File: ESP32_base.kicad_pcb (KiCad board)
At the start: 2 copper layers, 112 x 54.9 mm, 36 parts, among them J1 Conn_01x16_Socket, J2 Conn_01x16_Socket, J3 Conn_01x04_Socket, J4 USB_C_Receptacle_USB2.0_14P, J5 KH-IPEXA-SMAKWE-B080H, SW1 boot, SW2 reset, U1 ADT7310TRZ, U2 AP63203WU, U3 ESP32-C5-WROOM-1U-N8-R4

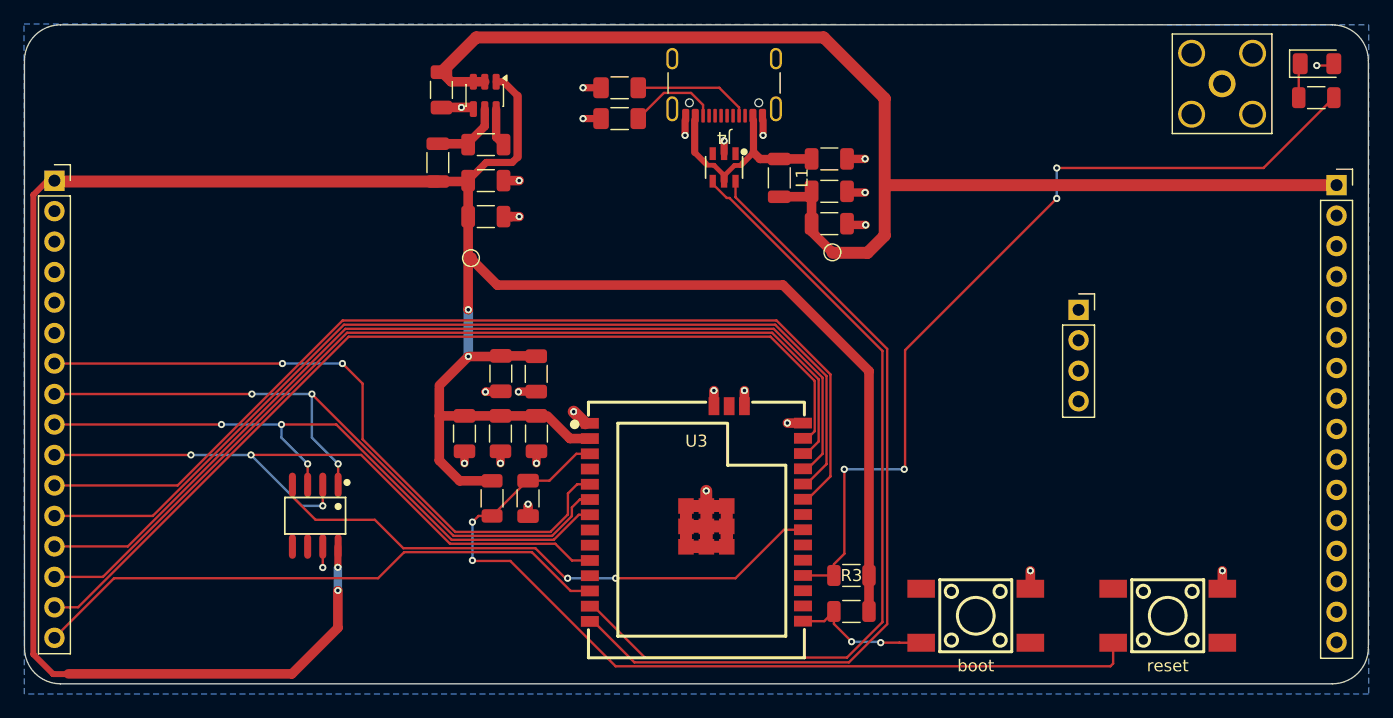
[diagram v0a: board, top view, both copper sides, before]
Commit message: fixed signal width at 0.3mm
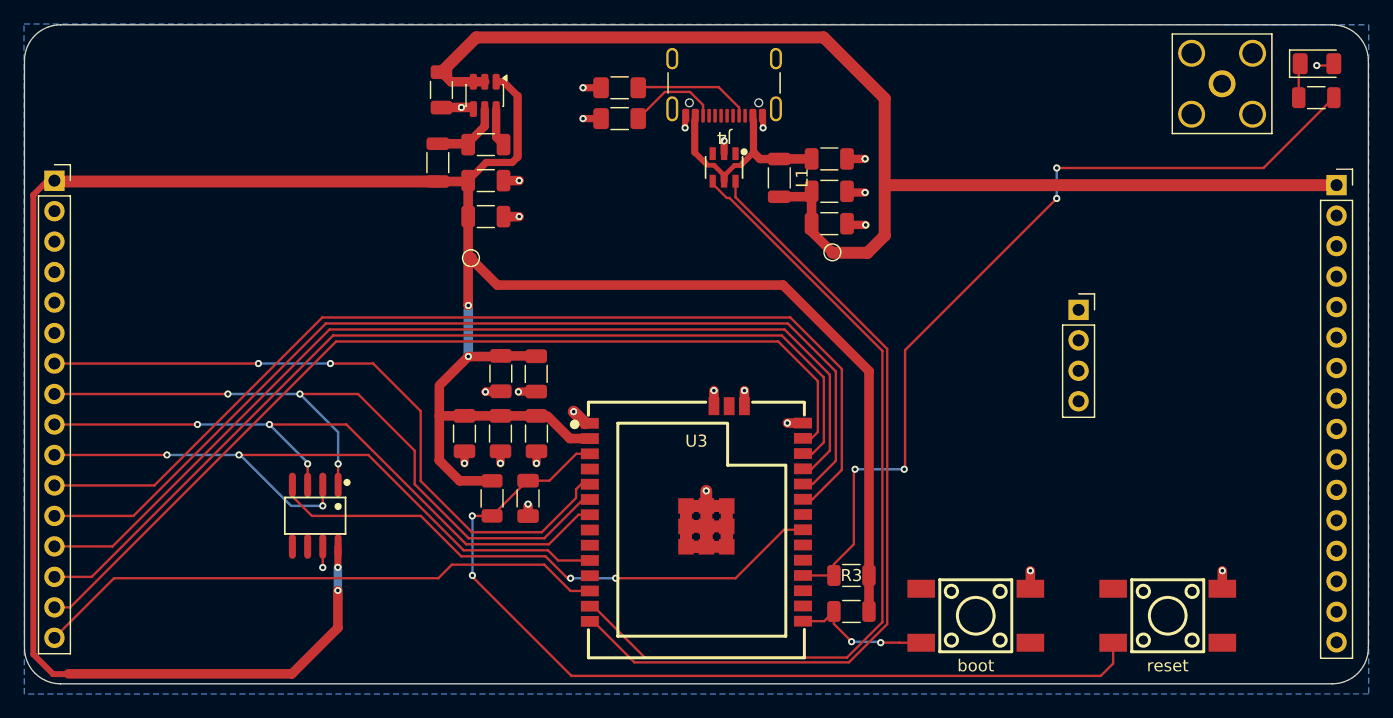
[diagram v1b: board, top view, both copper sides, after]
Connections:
- C1 pad 1: /USB_D+ -> Net-(C1-Pad1)
- J4 pad A4: /USB_D+ -> Net-(C1-Pad1)
- J4 pad A9: /USB_D+ -> Net-(C1-Pad1)
- J4 pad B4: /USB_D+ -> Net-(C1-Pad1)
- J4 pad B9: /USB_D+ -> Net-(C1-Pad1)
- L1 pad 1: /USB_D+ -> Net-(C1-Pad1)
- TVS1 pad 5: /USB_D+ -> Net-(C1-Pad1)
- TVS1 pad 6: /USB_D+ -> /USB_D-
- U3 pad 14: /USB_D+ -> /USB_D-
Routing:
- net /USB_D+: track 156.6 -> 69.6 mm
- net /USB_D-: track 0.00 -> 69.4 mm
- net Net-(C1-Pad1): track 0.00 -> 17.7 mm
- net /TP_IRQ: track 83.4 -> 85.5 mm
- net /TP_CS: track 82.4 -> 84.1 mm
- net Net-(U3-EN): track 73.9 -> 75.6 mm
- net /SPI_SCK: track 59.7 -> 61.3 mm
- net GND: track 63.2 -> 62.0 mm
- net /LCD_RST: track 81.3 -> 82.5 mm
- net /SPI_MISO: track 57.8 -> 58.8 mm
- net /SPI_MOSI: track 55.4 -> 56.3 mm
- net /LCD_DC: track 48.9 -> 48.1 mm
- net /LCD_CS: track 80.3 -> 81.1 mm

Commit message: wip
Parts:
- TVS1: footprint easyeda2kicad:SOT-23-6_L2.9-W1.6-P0.95-LS2.8-BL -> Package_TO_SOT_SMD:SOT-23-6
- turned TVS1 to -90 degrees
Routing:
- net /SPI_MISO: track 58.8 -> 64.9 mm
- net /SPI_MOSI: track 56.3 -> 62.4 mm
- net /SPI_SCK: track 61.3 -> 65.8 mm

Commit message: production ready #2
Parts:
- J4: value USB_C_Receptacle_USB2.0_14P -> USB_C_Receptacle_USB2.0_16P
- moved J4 0.20 mm to (141.9, 195.7)
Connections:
- J4 pad A8: (no net) -> unconnected-(J4-SBU1-PadA8)
- J4 pad B8: (no net) -> unconnected-(J4-SBU2-PadB8)
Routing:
- net Net-(J4-D+-PadA6): track 0.00 -> 6.13 mm
- net Net-(J4-D--PadA7): track 0.00 -> 5.80 mm

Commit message: wip
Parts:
- removed C10: 10uF, Capacitor_SMD:C_1206_3216Metric
- removed C11: 100nF, Capacitor_SMD:C_1206_3216Metric
- removed test_point1: 5V, TestPoint:TestPoint_Pad_D1.0mm
- removed test_point2: 3.3V, TestPoint:TestPoint_Pad_D1.0mm
- moved L1 4.67 mm to (150.8, 202.9), turned to 0 degrees
- moved L2 4.15 mm to (122.0, 204.6), turned to 180 degrees
- moved C1 3.01 mm to (150.8, 200.2)
- moved C6 2.20 mm to (122.0, 207.2)
- moved C7 1.80 mm to (122.0, 209.8)
- moved C13 0.71 mm to (120.2, 225.4), turned to -90 degrees
- moved C8 0.71 mm to (126.2, 225.4), turned to -90 degrees
- moved C9 0.71 mm to (123.2, 225.4), turned to -90 degrees
- moved C3 0.38 mm to (150.8, 208.2)
- moved C2 0.36 mm to (150.8, 205.5)
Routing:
- net Net-(C1-Pad1): track 17.9 -> 26.6 mm, vias 0 -> 2
- net +3.3V: track 226.5 -> 223.0 mm
- net GND: track 62.0 -> 64.2 mm, vias 26 -> 23
- net +5V: track 106.8 -> 105.6 mm
- net /USB_D+: track 69.8 -> 70.5 mm
- net Net-(U3-IO27): track 72.1 -> 72.7 mm

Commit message: production ready: 26.01.08
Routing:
- net Net-(U3-EN): track 75.8 -> 76.3 mm

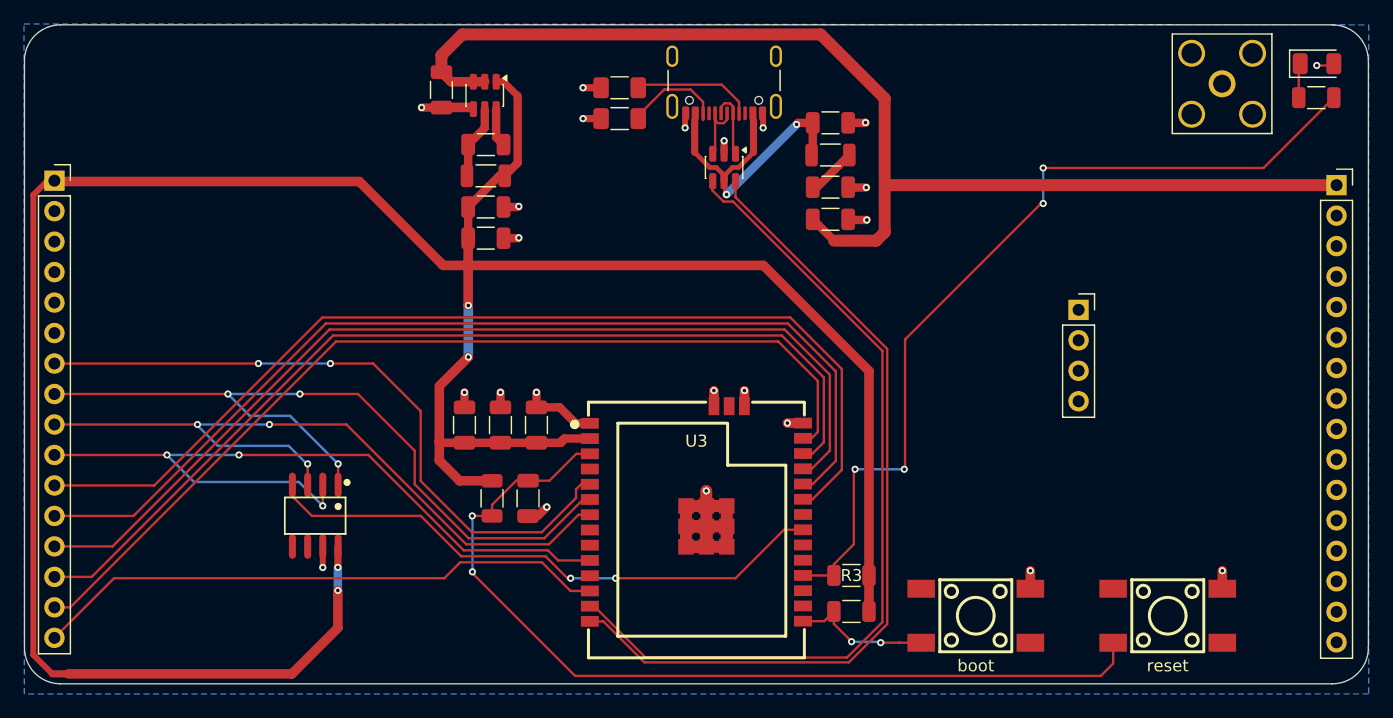
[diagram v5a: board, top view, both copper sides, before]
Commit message: replace power circuit
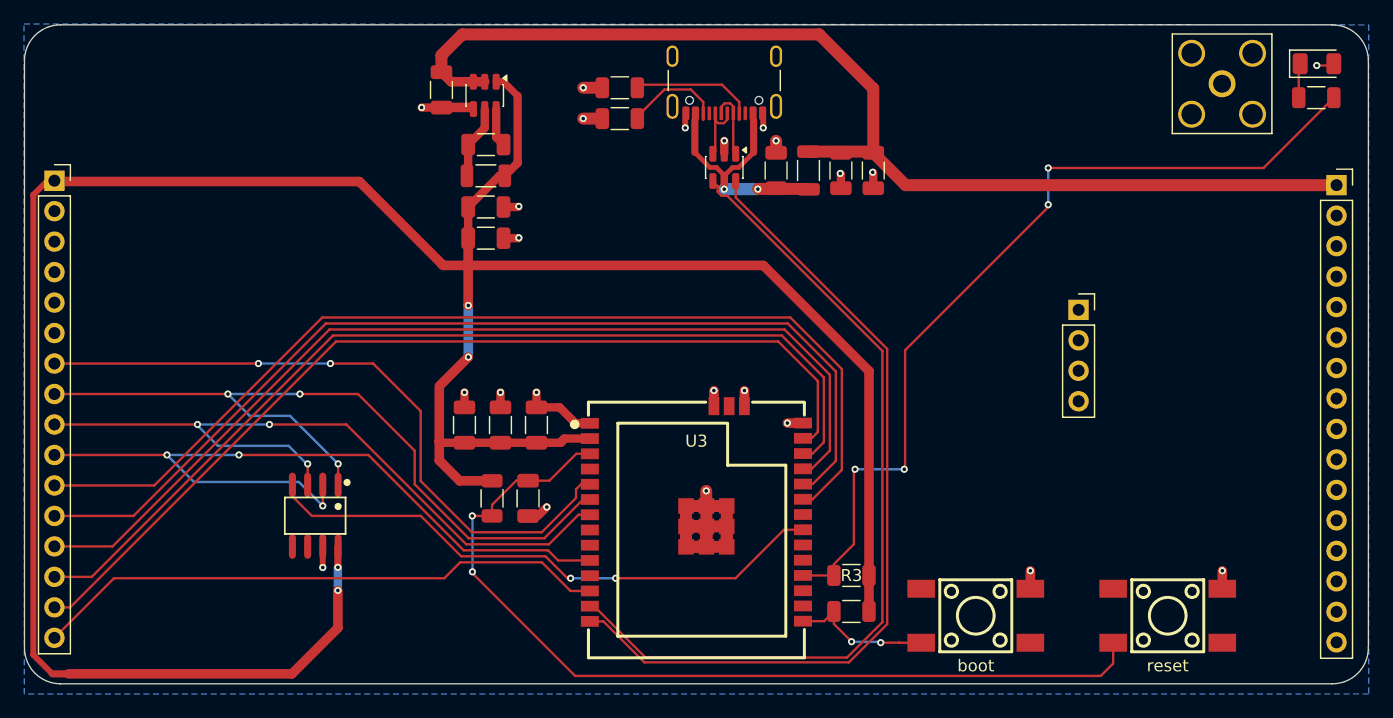
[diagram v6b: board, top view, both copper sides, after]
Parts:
- removed J4: USB_C_Receptacle_USB2.0_16P, Connector_USB:USB_C_Receptacle_GCT_USB4105-xx-A_16P_TopMnt_Horizontal
- removed TVS1: TVS, Package_TO_SOT_SMD:SOT-23-6
- added D60: USBLC6-2SC6, Package_TO_SOT_SMD:SOT-23-6, F.Cu at (141.9, 203.9)
- added J60: USB_C_Receptacle_USB2.0_16P, Connector_USB:USB_C_Receptacle_GCT_USB4105-xx-A_16P_TopMnt_Horizontal, F.Cu at (141.9, 195.7)
- R1, R2: footprint Resistor_SMD:R_1206_3216Metric_Pad1.30x1.75mm_HandSolder -> Resistor_SMD:R_1206_3216Metric
- moved C1 6.02 mm to (146.2, 204.2), turned to 90 degrees
- moved C3 5.41 mm to (154.3, 204.2), turned to -90 degrees
- moved L1 2.24 mm to (148.9, 204.2), turned to 90 degrees
- moved C2 1.64 mm to (151.6, 204.2), turned to -90 degrees
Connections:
- net Net-(C1-Pad1) renamed VBUS
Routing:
- net +5V: track 105.6 -> 94.5 mm
- net Net-(D60-Pad3): track 0.00 -> 6.13 mm
- net Net-(J4-D+-PadA6): track 6.13 -> 0.00 mm
- net Net-(J4-D--PadA7): track 5.80 -> 0.00 mm
- net Net-(D60-Pad1): track 0.00 -> 5.80 mm
- net VBUS: track 26.6 -> 20.8 mm
- net GND: track 64.4 -> 63.5 mm

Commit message: 0805
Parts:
- removed D60: USBLC6-2SC6, Package_TO_SOT_SMD:SOT-23-6
- removed J60: USB_C_Receptacle_USB2.0_16P, Connector_USB:USB_C_Receptacle_GCT_USB4105-xx-A_16P_TopMnt_Horizontal
- removed L1: CBW321609U601T, Inductor_SMD:L_1206_3216Metric
- removed L2: 4.7uH, Inductor_SMD:L_1206_3216Metric
- added FB1: 600, Inductor_SMD:L_0805_2012Metric, F.Cu at (147.7, 204.7)
- added FB2: 4.7uH, Capacitor_SMD:C_1210_3225Metric, F.Cu at (117.9, 202.7)
- added TVS1: USBLC6-2SC6, Package_TO_SOT_SMD:SOT-23-6, F.Cu at (142.0, 203.9)
- added USBC1: USB_C_Receptacle_USB2.0_16P, Connector_USB:USB_C_Receptacle_GCT_USB4105-xx-A_16P_TopMnt_Horizontal, F.Cu at (142.0, 195.7)
- C1, C12, C13, C2, C3, C4, C5, C6, C7, C8, C9: footprint Capacitor_SMD:C_1206_3216Metric -> Capacitor_SMD:C_0805_2012Metric
- LED1: footprint LED_SMD:LED_1206_3216Metric -> LED_SMD:LED_0805_2012Metric
- R1, R2: footprint Resistor_SMD:R_1206_3216Metric -> Resistor_SMD:R_0805_2012Metric
- R3, R4, R5, R7: footprint Resistor_SMD:R_1206_3216Metric -> PCM_JLCPCB:R_0805
- U2: value AP63203WU -> 3.3V
- moved C7 3.91 mm to (121.4, 205.9)
- moved C6 3.61 mm to (121.4, 203.6)
- moved R7 3.56 mm to (124.9, 228.8), turned to 0 degrees
- moved C12 3.01 mm to (127.9, 229.6)
- moved C13 2.98 mm to (123.2, 224.7), turned to 90 degrees
- moved C9 2.35 mm to (125.5, 224.7)
- moved C3 2.18 mm to (152.2, 204.7), turned to 90 degrees
- moved C2 1.80 mm to (149.9, 204.7), turned to 90 degrees
- moved C8 1.73 mm to (127.8, 224.7)
- moved R2 1.04 mm to (134.1, 199.4)
- moved R5 0.99 mm to (151.8, 241.6)
- moved R1 0.95 mm to (134.1, 197.3)
- moved C1 0.92 mm to (145.5, 204.7)
- moved C5 0.91 mm to (121.4, 201.3)
- moved R3 0.70 mm to (151.8, 237.9)
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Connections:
- C13 pad 1: GND -> +3.3V
- C13 pad 2: +3.3V -> GND
- LED1 pad 1: Net-(LED1-A) -> GND
- LED1 pad 2: GND -> Net-(LED1-A)
- R7 pad 1: Net-(U3-EN) -> +3.3V
- R7 pad 2: +3.3V -> Net-(U3-EN)
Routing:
- net Net-(U3-IO27): track 72.5 -> 86.3 mm, vias 4 -> 2
- net +5V: track 94.5 -> 101.9 mm
- net Net-(D60-Pad3): track 6.13 -> 0.00 mm
- net Net-(TVS1-Pad1): track 0.00 -> 5.80 mm
- net Net-(D60-Pad1): track 5.80 -> 0.00 mm
- net +3.3V: track 223.0 -> 228.7 mm
- net Net-(TVS1-Pad3): track 0.00 -> 5.69 mm
- net GND: track 63.5 -> 58.1 mm, vias 23 -> 24
- net Net-(U3-EN): track 76.3 -> 71.6 mm
- net Net-(U2-SW): track 6.25 -> 5.28 mm
- net Net-(U2-BST): track 3.22 -> 2.28 mm
- net Net-(USBC1-CC1): track 10.5 -> 9.69 mm
- net Net-(USBC1-CC2): track 8.50 -> 7.68 mm
- net /USB_D-: track 69.4 -> 70.2 mm
- net VBUS: track 20.8 -> 20.2 mm
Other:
- board text added: "LCD"
- board text added: "SD card"
- board text added: "SPI"
- board text added: "shield ext."
- board text added: "v.e938d34"
- board text removed: "v.6e07b40"

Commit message: pre spreading signals
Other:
- board text added: "v.4fa88d8"
- board text removed: "v.e938d34"
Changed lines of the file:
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@@
 		)
 	)
-	(gr_text "v.e938d34"
+	(gr_text "v.4fa88d8"
 		(at 189.55 245.6 0)
 		(layer "B.SilkS")
@@
 	)
 	(segment
+		(start 127.8 227)
+		(end 125.5 227)
+		(width 0.7)
+		(layer "F.Cu")
+		(net 2)
+	)
+	(segment
 		(start 120.45 206.4625)
 		(end 120.45 205.9375)
@@
 		(layer "F.Cu")
 		(net 2)
-	)
-	(segment
-		(start 127.8 227)
-		(end 125.5 227)
-		(width 0.7)
-		(layer "F.Cu")
-		(net 2)
